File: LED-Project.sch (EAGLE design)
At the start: 8 parts, among them U1 IS31FL3236A, U2 MSP430G2132

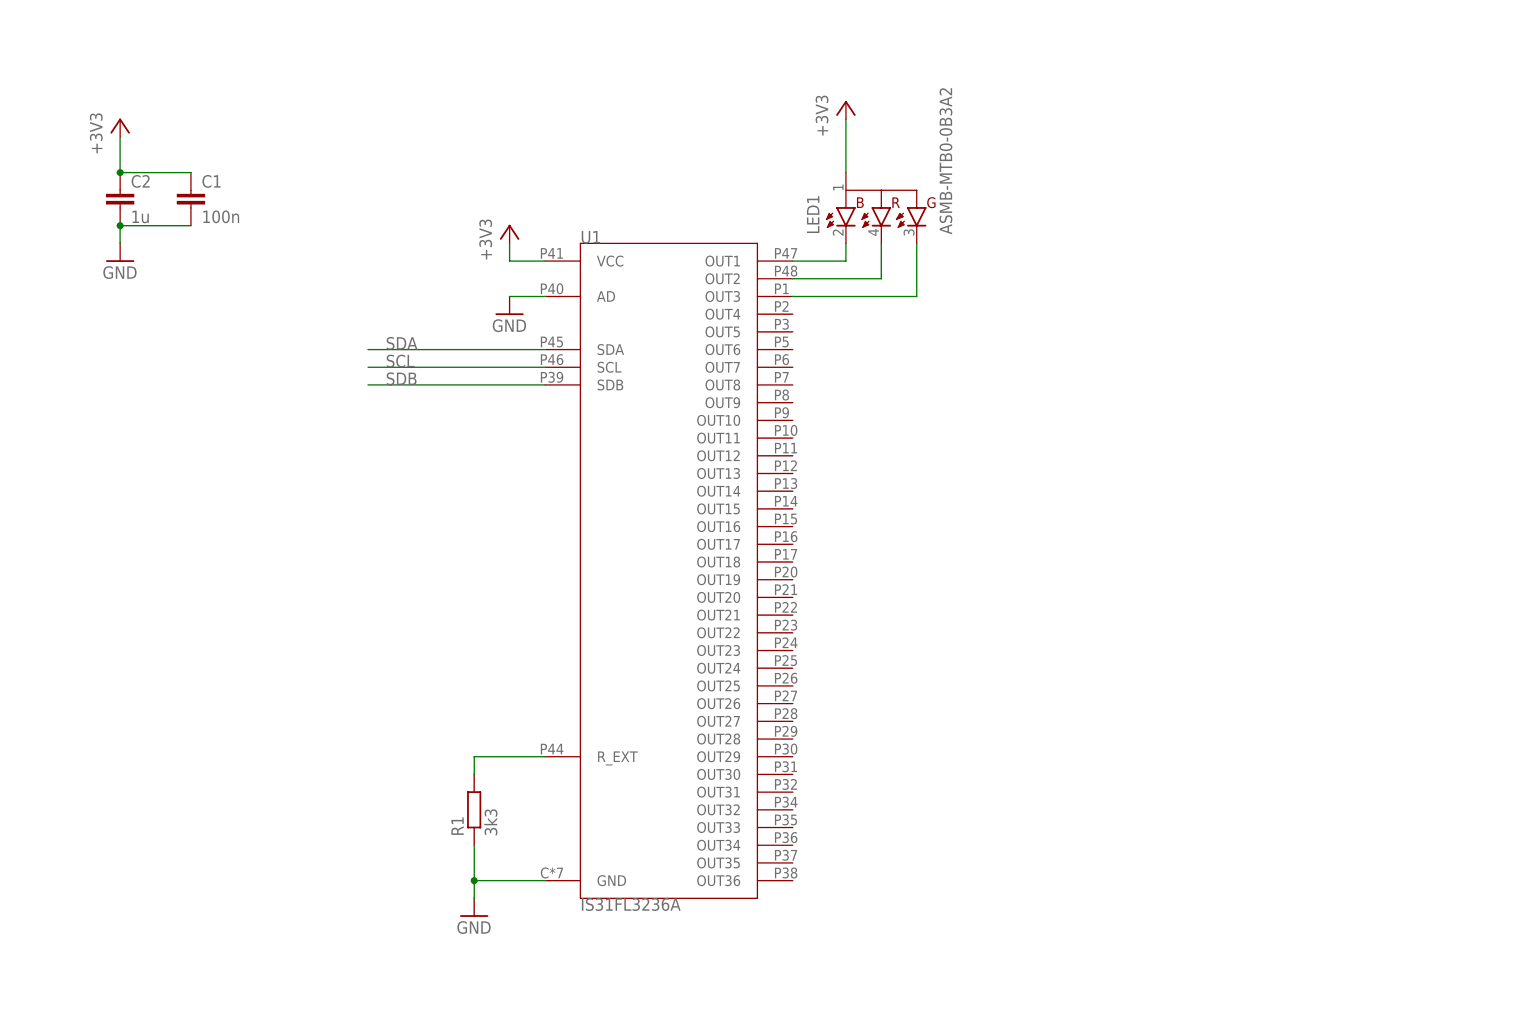
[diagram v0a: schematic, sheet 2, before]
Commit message: add solar and battery
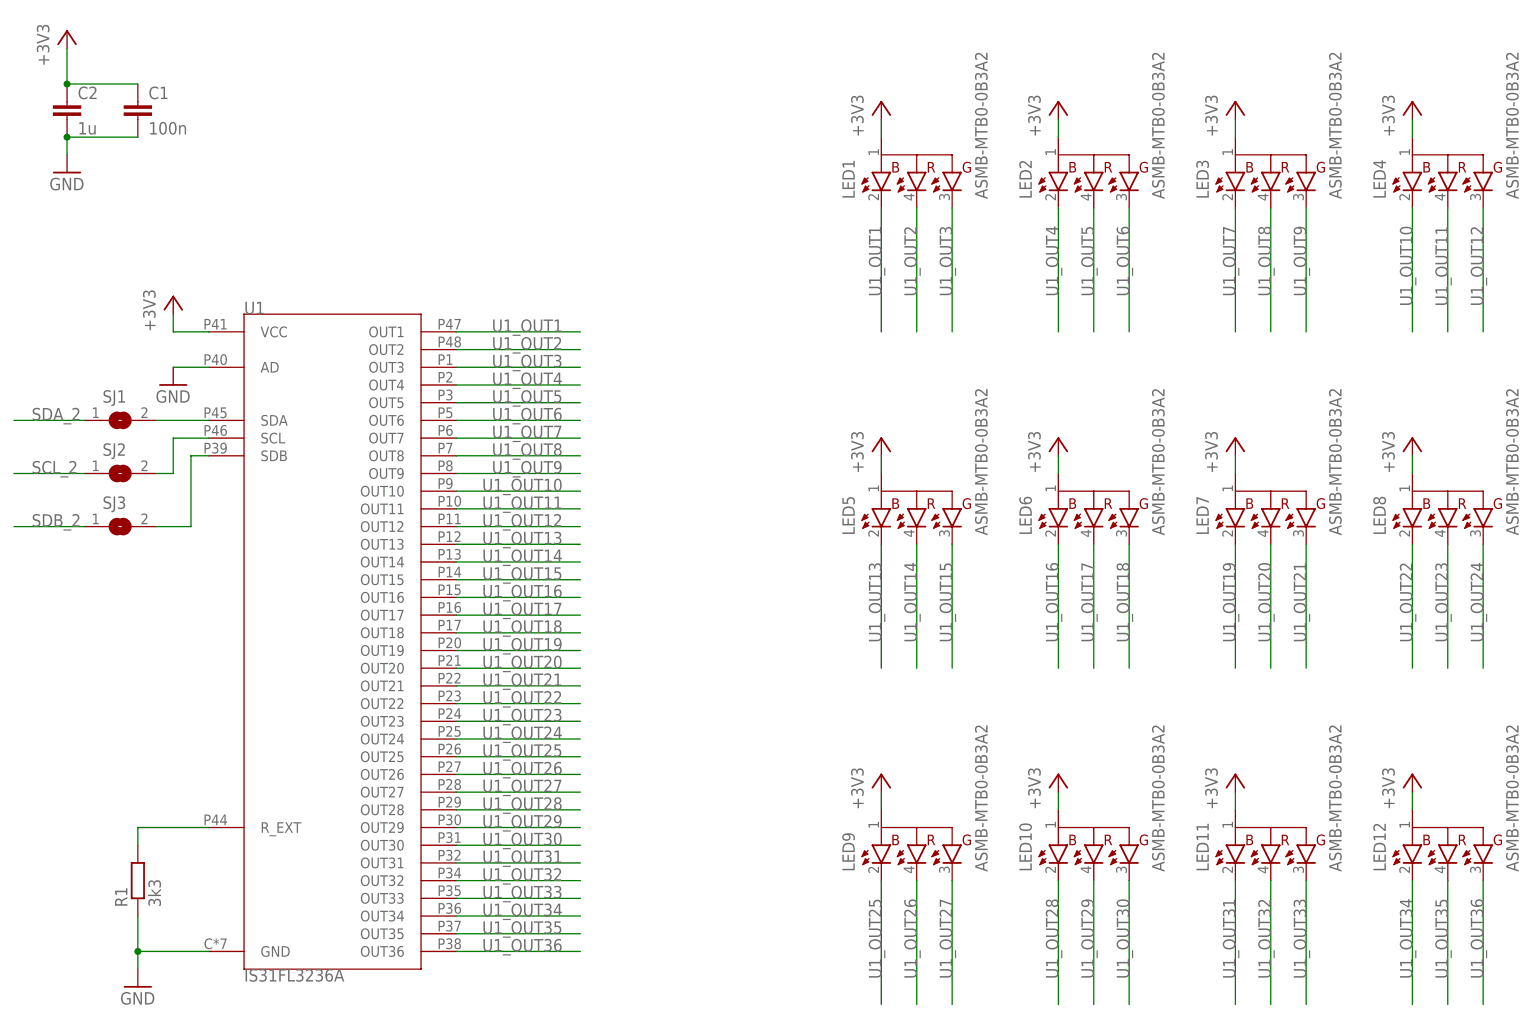
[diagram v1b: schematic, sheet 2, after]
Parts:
- added LED10, LED11, LED12, LED2, LED3, LED4, LED5, LED6, LED7, LED8, LED9: ASMB-MTB0-0B3A2, LED-Project:ASMB-MTB0-0B3A2
- added SJ1, SJ2, SJ3: (no value), jumper:SJ
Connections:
- net N$1 renamed U1_OUT1
- net N$2 renamed U1_OUT2
- net N$3 renamed U1_OUT3
- new net SCL_2: SJ2.1
- new net SDA_2: SJ1.1
- new net SDB_2: SJ3.1
- new net U1_OUT10: LED4.BC, U1.OUT10
- new net U1_OUT11: LED4.RC, U1.OUT11
- new net U1_OUT12: LED4.GC, U1.OUT12
- new net U1_OUT13: LED5.BC, U1.OUT13
- new net U1_OUT14: LED5.RC, U1.OUT14
- new net U1_OUT15: LED5.GC, U1.OUT15
- new net U1_OUT16: LED6.BC, U1.OUT16
- new net U1_OUT17: LED6.RC, U1.OUT17
- new net U1_OUT18: LED6.GC, U1.OUT18
- new net U1_OUT19: LED7.BC, U1.OUT19
- new net U1_OUT20: LED7.RC, U1.OUT20
- new net U1_OUT21: LED7.GC, U1.OUT21
- new net U1_OUT22: LED8.BC, U1.OUT22
- new net U1_OUT23: LED8.RC, U1.OUT23
- new net U1_OUT24: LED8.GC, U1.OUT24
- new net U1_OUT25: LED9.BC, U1.OUT25
- new net U1_OUT26: LED9.RC, U1.OUT26
- new net U1_OUT27: LED9.GC, U1.OUT27
- new net U1_OUT28: LED10.BC, U1.OUT28
- new net U1_OUT29: LED10.RC, U1.OUT29
- new net U1_OUT30: LED10.GC, U1.OUT30
- new net U1_OUT31: LED11.BC, U1.OUT31
- new net U1_OUT32: LED11.RC, U1.OUT32
- new net U1_OUT33: LED11.GC, U1.OUT33
- new net U1_OUT34: LED12.BC, U1.OUT34
- new net U1_OUT35: LED12.RC, U1.OUT35
- new net U1_OUT36: LED12.GC, U1.OUT36
- new net U1_OUT4: LED2.BC, U1.OUT4
- new net U1_OUT5: LED2.RC, U1.OUT5
- new net U1_OUT6: LED2.GC, U1.OUT6
- new net U1_OUT7: LED3.BC, U1.OUT7
- new net U1_OUT8: LED3.RC, U1.OUT8
- new net U1_OUT9: LED3.GC, U1.OUT9
- net +3V3: now also LED10.P$1, LED11.P$1, LED12.P$1, LED2.P$1, LED3.P$1, LED4.P$1, LED5.P$1, LED6.P$1, LED7.P$1, LED8.P$1, LED9.P$1
- net SCL: now also SJ2.2
- net SDA: now also SJ1.2
- net SDB: now also SJ3.2
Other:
- moved on the sheet: C1, C2, LED1, R1, U1
